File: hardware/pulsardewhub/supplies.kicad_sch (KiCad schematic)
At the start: 24 parts, among them U20 LMR33630ADDA, U30 LMR33630ADDA

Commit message: Reduce PulsarPower power-path cost while retaining current monitoring
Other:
- title: PulsarDew Hub - 5 V USB and 3.3 V logic supplies -> PulsarPower - 5 V USB and 3.3 V logic supplies
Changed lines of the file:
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@@
 (kicad_sch (version 20260306) (generator "eeschema") (generator_version "10.0") (paper "A3")
-(title_block (title "PulsarDew Hub - 5 V USB and 3.3 V logic supplies") (date "2026-10-03") (rev "0.2-draft") (company "PulsarFab"))
+(title_block (title "PulsarPower - 5 V USB and 3.3 V logic supplies") (date "2026-10-03") (rev "0.3-draft") (company "PulsarFab"))
 (text "DC SUPPLIES | LMR33630ADDA, 400 kHz | 5 V / 3 A + 3.3 V logic" (at 20.3200 16.5100 0) (effects (font (size 2 2)) (justify left top)))
 (hierarchical_label "VIN" (shape input) (at 25.4000 35.5600 0) (effects (font (size 1.27 1.27)) (justify left bottom)))

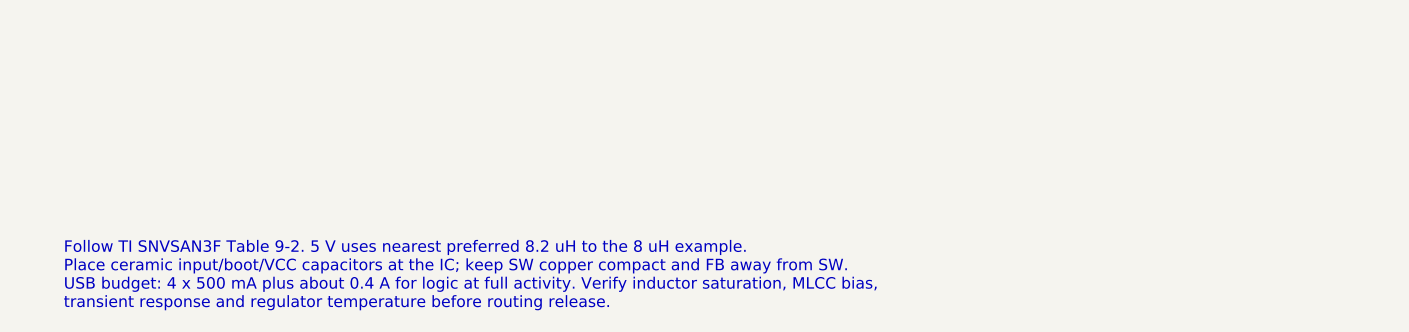
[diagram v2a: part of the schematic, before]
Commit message: Use owned XKB barrel sockets and evaluate LMR51610 commonality
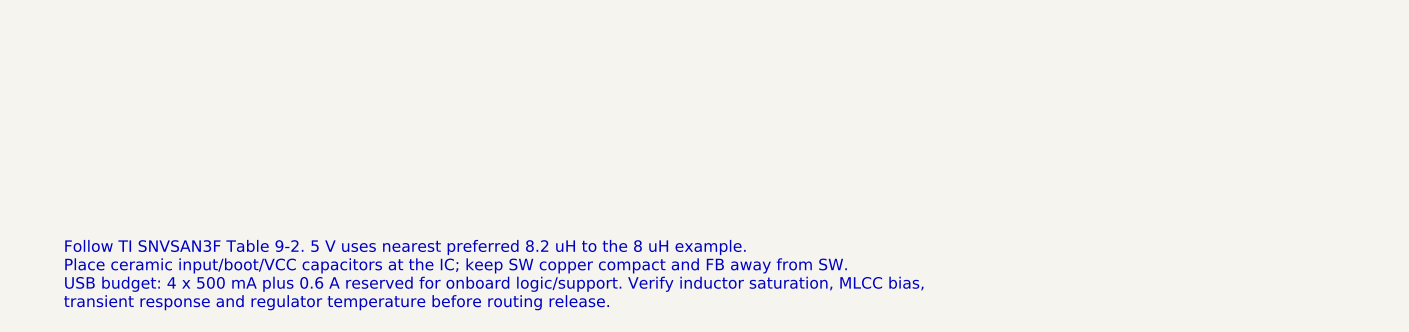
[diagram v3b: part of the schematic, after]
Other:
- note added: "Follow TI SNVSAN3F Table 9-2. 5 V uses nearest preferred 8.2 uH to the 8 uH example. Place ceramic input/boot/VCC capacitors at the IC; keep SW copper compact and FB away from SW. USB budget: 4 x 500 mA plus 0.6 A reserved for onboard logic/support. Verify inductor saturation, MLCC bias, transient response and regulator temperature before routing release."
- note removed: "Follow TI SNVSAN3F Table 9-2. 5 V uses nearest preferred 8.2 uH to the 8 uH example. Place ceramic input/boot/VCC capacitors at the IC; keep SW copper compact and FB away from SW. USB budget: 4 x 500 mA plus about 0.4 A for logic at full activity. Verify inductor saturation, MLCC bias, transient response and regulator temperature before routing release."
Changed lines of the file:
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@@
         (unit 1)))))
 (label "V3"  (at 355.6000 175.2600 0) (effects (font (size 1.27 1.27)) (justify left bottom)))
-(text "Follow TI SNVSAN3F Table 9-2. 5 V uses nearest preferred 8.2 uH to the 8 uH example.\nPlace ceramic input/boot/VCC capacitors at the IC; keep SW copper compact and FB away from SW.\nUSB budget: 4 x 500 mA plus about 0.4 A for logic at full activity. Verify inductor saturation, MLCC bias,\ntransient response and regulator temperature before routing release." (at 25.4000 254.0000 0) (effects (font (size 1.27 1.27)) (justify left top)))
+(text "Follow TI SNVSAN3F Table 9-2. 5 V uses nearest preferred 8.2 uH to the 8 uH example.\nPlace ceramic input/boot/VCC capacitors at the IC; keep SW copper compact and FB away from SW.\nUSB budget: 4 x 500 mA plus 0.6 A reserved for onboard logic/support. Verify inductor saturation, MLCC bias,\ntransient response and regulator temperature before routing release." (at 25.4000 254.0000 0) (effects (font (size 1.27 1.27)) (justify left top)))
 (wire (pts (xy 25.4000 35.5600) (xy 45.7200 35.5600)) (stroke (width 0) (type default)))
 (wire (pts (xy 25.4000 43.1800) (xy 45.7200 43.1800)) (stroke (width 0) (type default)))

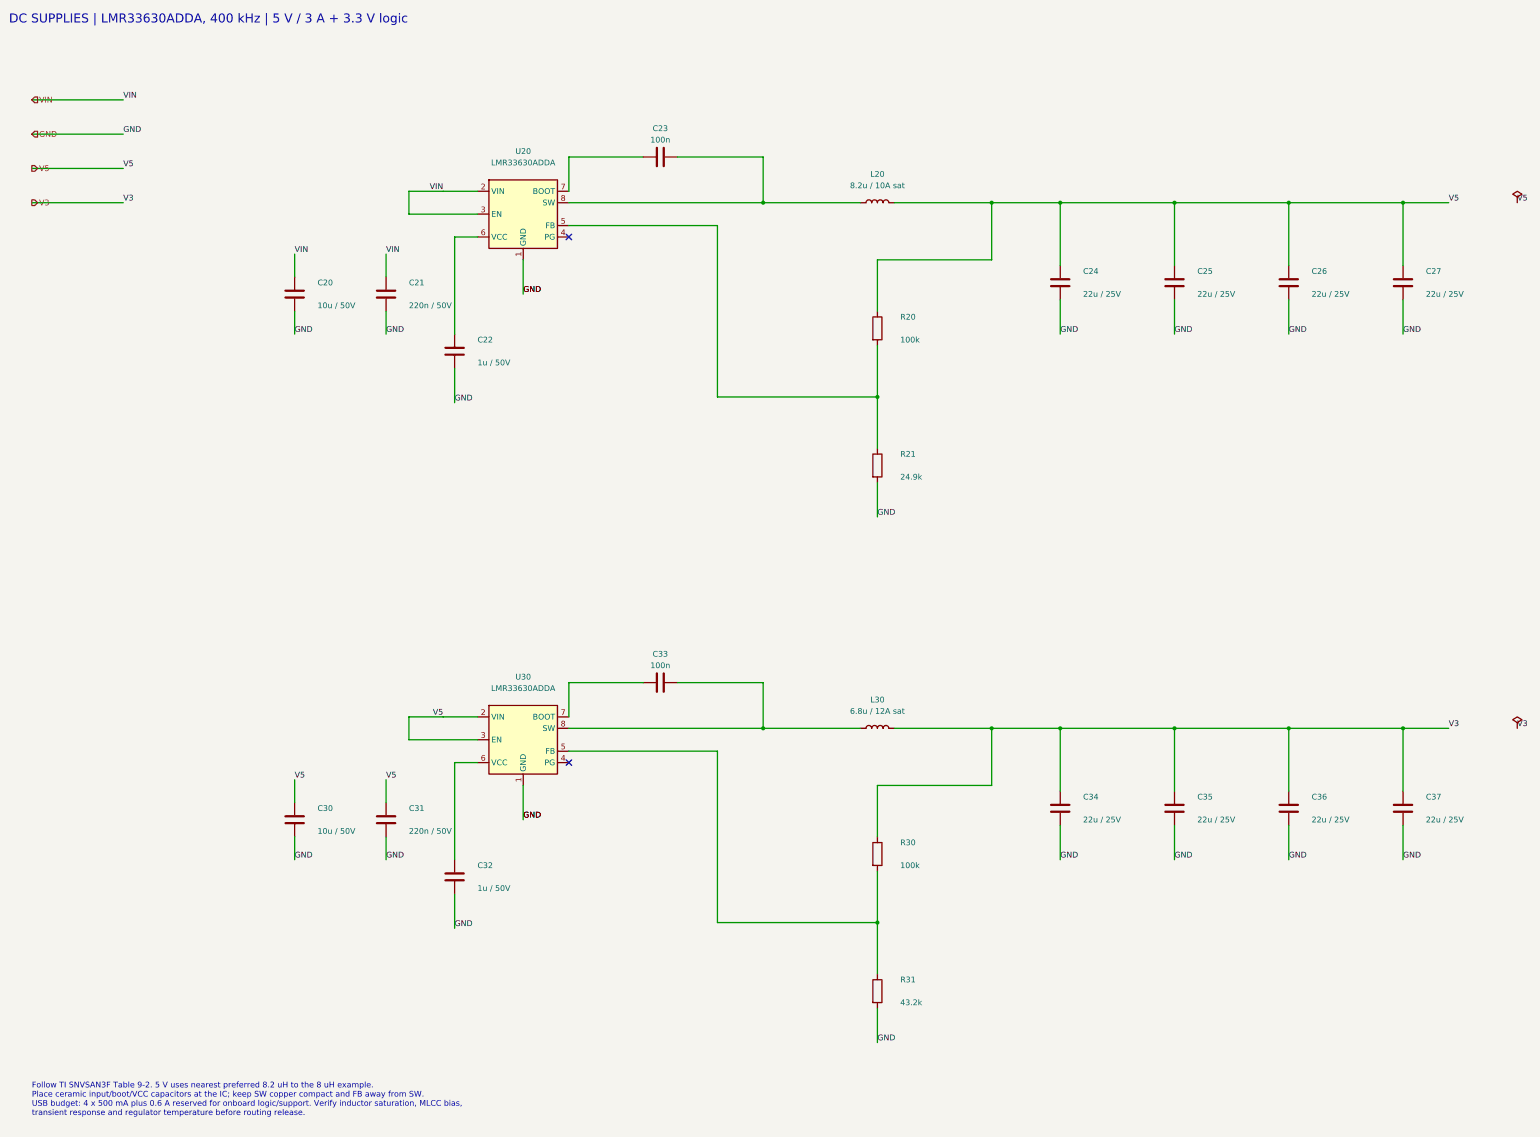
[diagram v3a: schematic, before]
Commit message: Use owned LMR51610 for PulsarPower 3.3 V logic supply
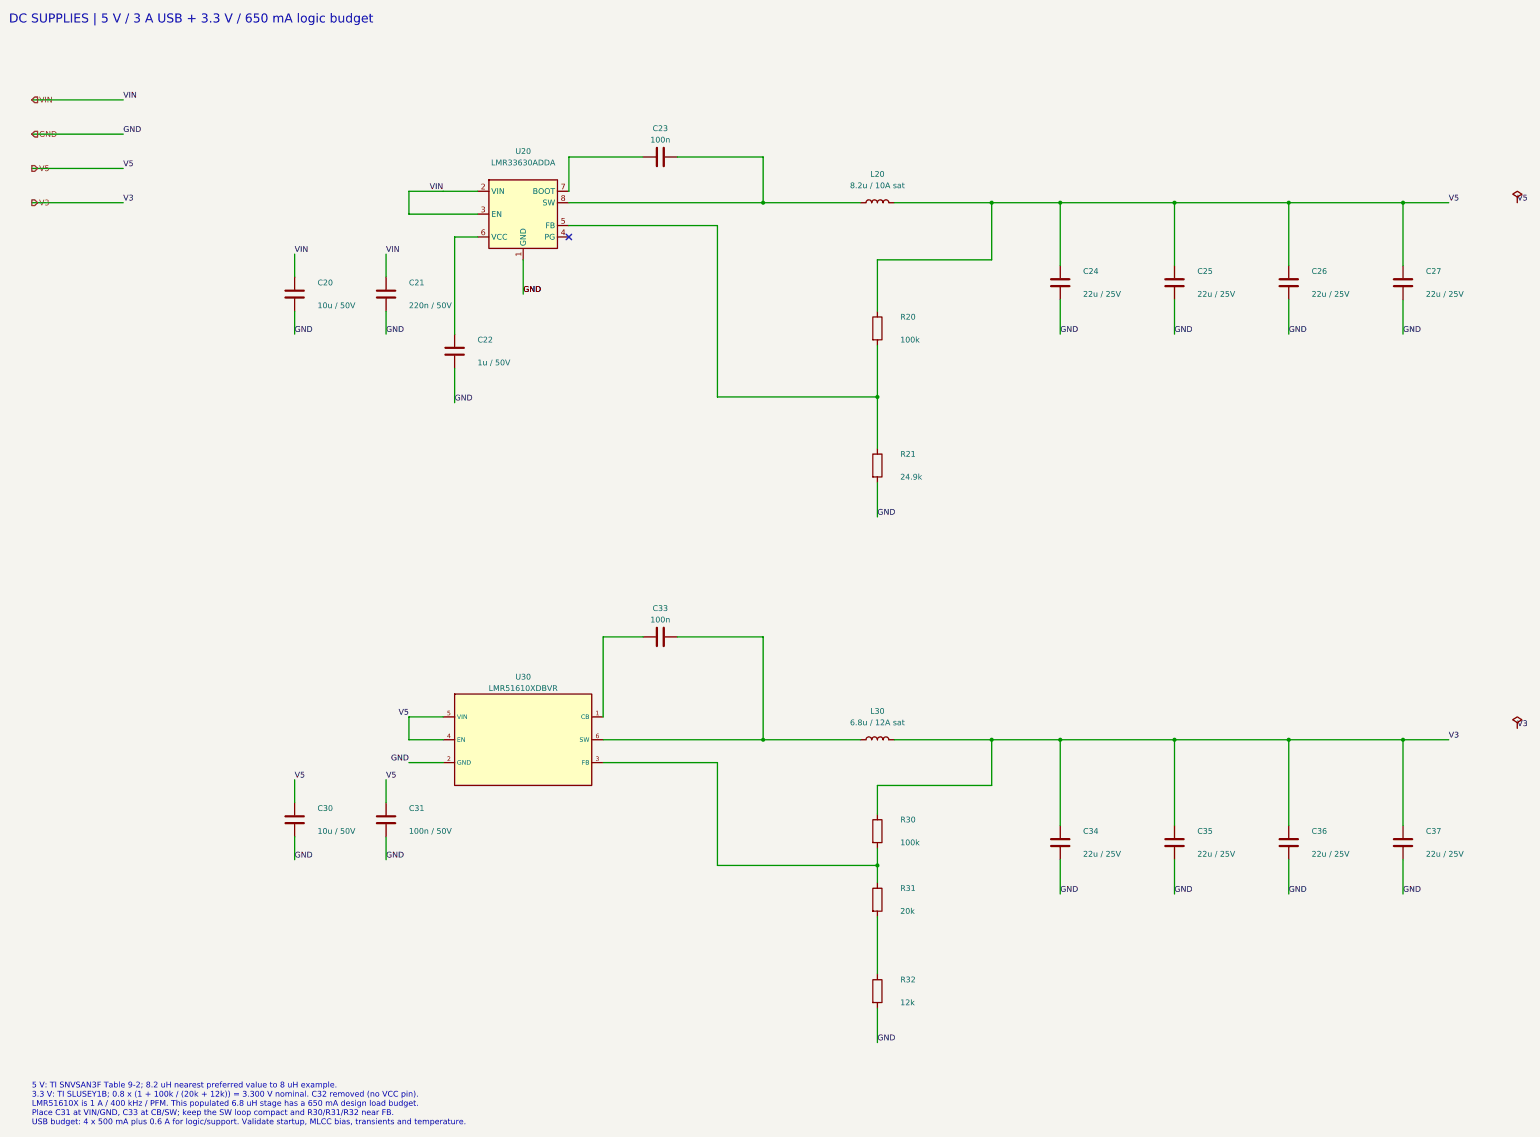
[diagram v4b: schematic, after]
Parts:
- removed C32: 1u / 50V, Capacitor_SMD:C_0603_1608Metric, symbol Device:C
- added R32: 12k, Resistor_SMD:R_0603_1608Metric, symbol Device:R
- C31: value 220n / 50V -> 100n / 50V; LCSC C64705 -> C14663; MPN CL10B224KB8NNNC -> CC0603KRX7R9BB104; Manufacturer Samsung Electro-Mechanics -> YAGEO
- R31: value 43.2k -> 20k; LCSC C23053 -> C4184; MPN 0603WAF4322T5E -> 0603WAF2002T5E
- U30: value LMR33630ADDA -> LMR51610XDBVR; footprint Package_SO:Texas_HSOP-8-1EP_3.9x4.9mm_P1.27mm -> Package_TO_SOT_SMD:SOT-23-6; symbol Regulator_Switching:LMR33630ADDA -> pulsarfab_hub:LMR51610XDBV; LCSC C841384 -> C20539658; MPN LMR33630ADDAR -> LMR51610XDBVR; Manufacturer TI -> Texas Instruments
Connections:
- net GND: now also U30.2 (GND), R32.2; no longer R31.2, U30.1 (GND), U30.9 (GND)
- net V5: now also U30.4 (EN), U30.5 (VIN); no longer U30.2 (VIN), U30.3 (EN)
- net at R30.2, R31.1: now also U30.3 (FB); no longer U30.5 (FB)
- net at C33.1: now also U30.1 (CB); no longer U30.7 (BOOT)
- net at C33.2, L30.1: now also U30.6 (SW); no longer U30.8 (SW)
- new net: R31.2, R32.1
- no-connect marks 2 -> 1
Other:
- note added: "5 V: TI SNVSAN3F Table 9-2; 8.2 uH nearest preferred value to 8 uH example. 3.3 V: TI SLUSEY1B; 0.8 x (1 + 100k / (20k + 12k)) = 3.300 V nominal. C32 removed (no VCC pin). LMR51610X is 1 A / 400 kHz / PFM. This populated 6.8 uH stage has a 650 mA design load budget. Place C31 at VIN/GND, C33 at CB/SW; keep the SW loop compact and R30/R31/R32 near FB. USB budget: 4 x 500 mA plus 0.6 A for logic/su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"
- note added: "DC SUPPLIES | 5 V / 3 A USB + 3.3 V / 650 mA logic budget"
- note removed: "DC SUPPLIES | LMR33630ADDA, 400 kHz | 5 V / 3 A + 3.3 V logic"
- note removed: "Follow TI SNVSAN3F Table 9-2. 5 V uses nearest preferred 8.2 uH to the 8 uH example. Place ceramic input/boot/VCC capacitors at the IC; keep SW copper compact and FB away from SW. USB budget: 4 x 500 mA plus 0.6 A reserved for onboard logic/support. Verify inductor saturation, MLCC bias, transient response and regulator temperature before routing release."
- moved on the sheet: C33, C34, C35, C36, C37, L30, R30, R31
